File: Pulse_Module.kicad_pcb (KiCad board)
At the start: 2 copper layers, 61 parts, among them CON1 AVR-ISP-10, CON2 AVR-JTAG-10, CON3 BARREL_JACK, IC1 ATMEGA1280-A, P1 CONN_02X20, P2 USB_OTG, P3 CONN_01X03, P4 CONN_01X03, SW1 SW_PUSH, U1 74HCT541_PWR, U2 PL2303, U6 WS2812, U7 WS2812, U8 WS2812, X1 CRYSTAL, Y1 CRYSTAL

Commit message: Готовая плата версия_1
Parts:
- removed C15, C18: 0.1uF, Capacitors_SMD:C_0805
- removed R10: 150, Resistors_SMD:R_0402
- added C17: 0.1U, Capacitors_SMD:C_0805, F.Cu at (142.2, 117.8)
- moved P2 67.4 mm to (142.1, 145.7), turned to 0 degrees
- moved R3 62.8 mm to (143.2, 140.0), turned to 270 degrees
- moved C13 60.0 mm to (171.9, 134.2)
- moved D1 59.2 mm to (156.7, 134.0), turned to 90 degrees
- moved U7 58.2 mm to (185.6, 140.2), turned to 90 degrees
- moved U6 58.0 mm to (179.6, 140.2), turned to 90 degrees
- moved U8 57.9 mm to (173.6, 140.2), turned to 90 degrees
- moved R1 56.9 mm to (159.7, 134.1), turned to 90 degrees
- moved R4 56.3 mm to (140.2, 140.0), turned to 270 degrees
- moved D3 55.8 mm to (150.7, 134.0), turned to 90 degrees
- moved R5 55.7 mm to (146.0, 140.0), turned to 90 degrees
- moved C8 55.1 mm to (177.9, 134.2)
- moved R7 48.1 mm to (147.8, 134.1), turned to 90 degrees
- moved C7 47.4 mm to (183.9, 134.2), turned to 90 degrees
- moved R12 45.9 mm to (156.7, 129.7)
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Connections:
- net /Sheet56DEE0DD/17 renamed Net-(IC1-Pad35)
- C1 pad 1: /Vcc -> /Sheet56DEE0DD/Vcc
- C2 pad 1: /Vcc -> /Sheet56DEE0DD/Vcc
- CON1 pad 5: /Sheet56DEE0DD/RESET -> /Sheet56DEE0DD/Sheet570520A0/RESET
- Cff1 pad 1: /Vcc -> /Sheet56DEE0DD/Vcc
- IC1 pad 2: /Sheet56DEE0DD/RXD -> /Sheet56DEE0DD/Sheet570520A0/RXD
- IC1 pad 3: /Sheet56DEE0DD/TXD -> /Sheet56DEE0DD/Sheet570520A0/TXD
- IC1 pad 30: /Sheet56DEE0DD/RESET -> /Sheet56DEE0DD/Sheet570520A0/RESET
- JP2 pad 2: Net-(JP2-Pad2) -> /Sheet56D88A8D/FB
- JP2 pad 3: /Sheet56D88A8D/FB -> Net-(JP2-Pad3)
- L1 pad 2: /Vcc -> /Sheet56DEE0DD/Vcc
- P4 pad 2: /Sheet56DEE0DD/TXD -> /Sheet56DEE0DD/Sheet570520A0/TXD
- P4 pad 3: /Sheet56DEE0DD/RXD -> /Sheet56DEE0DD/Sheet570520A0/RXD
- R14 pad 1: /Vcc -> /Sheet56DEE0DD/Vcc
- R15 pad 1: Net-(JP2-Pad1) -> Net-(JP2-Pad3)
- R6 pad 2: /Sheet56DEE0DD/RESET -> /Sheet56DEE0DD/Sheet570520A0/RESET
- R9 pad 1: Net-(JP2-Pad2) -> Net-(JP2-Pad1)
- SW1 pad 2: /Sheet56DEE0DD/RESET -> /Sheet56DEE0DD/Sheet570520A0/RESET
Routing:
- net GND: track 1.59 -> 320.2 mm, vias 0 -> 21
- net +5V: track 166.9 -> 314.5 mm
- net /Sheet56DEE0DD/Sheet570520A0/RESET: track 0.00 -> 88.8 mm, vias 0 -> 5
- net /Sheet56DEE0DD/Dout: track 0.00 -> 81.4 mm, vias 0 -> 4
- net /Sheet56DEE0DD/Vcc: track 0.00 -> 68.3 mm
- net /Sheet56DEE0DD/CS: track 0.00 -> 65.0 mm, vias 0 -> 4
- net /Sheet56DEE0DD/Sheet570520A0/RXD: track 0.00 -> 57.2 mm, vias 0 -> 2
- net /Sheet56DEE0DD/Sheet570520A0/TXD: track 0.00 -> 55.6 mm, vias 0 -> 2
- net /Sheet56DEE0DD/40: track 0.00 -> 50.0 mm
- net Net-(IC1-Pad63): track 0.00 -> 50.0 mm, vias 0 -> 4
- net /Vcc: track 47.5 -> 0.00 mm, vias 4 -> 0
- net /Sheet56DEE0DD/Sheet570520A0/D+: track 0.00 -> 46.8 mm
- net /Sheet56DEE0DD/Sheet570520A0/D-: track 0.00 -> 45.7 mm
- net /Sheet56DEE0DD/38: track 0.00 -> 44.3 mm
- net /Sheet56DEE0DD/36: track 0.00 -> 43.3 mm, vias 0 -> 1
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- added copper zone on B.Cu, net GND
- added copper zone on F.Cu, net GND
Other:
- board outline added: 100.2 x 67.8 mm
- net class Pit added: clearance 0.1, trace_width 0.4, via_dia 0.6, via_drill 0.4
- net class Power added: clearance 0.1, trace_width 0.8, via_dia 0.6, via_drill 0.4

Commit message: Переразведённая лмка
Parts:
- added REF**: 1pin, Connect:1pin, F.Cu at (199.4, 81.9)
- moved REF** 186.6 mm to (106.7, 146.7)
- moved REF** 153.5 mm to (106.7, 81.9)
- moved REF** 102.8 mm to (199.4, 146.7)
- moved C1 27.4 mm to (127.1, 133.1), turned to 0 degrees
- moved D2 21.5 mm to (107.6, 118.0)
- moved C2 19.1 mm to (132.5, 107.4)
- moved LM2596 14.6 mm to (117.6, 105.3)
- moved R14 14.6 mm to (126.2, 103.5)
- moved Cff1 12.1 mm to (126.3, 99.9)
- moved L1 10.7 mm to (127.1, 118.5), turned to 0 degrees
- moved R15 9.08 mm to (112.6, 95.6)
- moved JP2 3.73 mm to (120.1, 92.8)
- moved CON3 2.18 mm to (117.6, 140.9)
- moved R9 1.83 mm to (127.4, 95.0), turned to 270 degrees
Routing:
- net /Sheet56D88A8D/FB: track 54.7 -> 23.1 mm
- net /Sheet56D88A8D/Vin: track 12.6 -> 26.2 mm
- net +5V: track 314.5 -> 304.0 mm, vias 0 -> 2
- net GND: track 320.2 -> 309.7 mm
- net Net-(D2-Pad2): track 22.2 -> 31.7 mm
- net (no net): track 9.41 -> 0.00 mm
- net /Sheet56DEE0DD/Vcc: track 68.3 -> 64.3 mm
- net Net-(JP2-Pad1): track 3.30 -> 5.26 mm
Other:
- board size 100.2 x 67.8 mm -> 100.2 x 70.9 mm

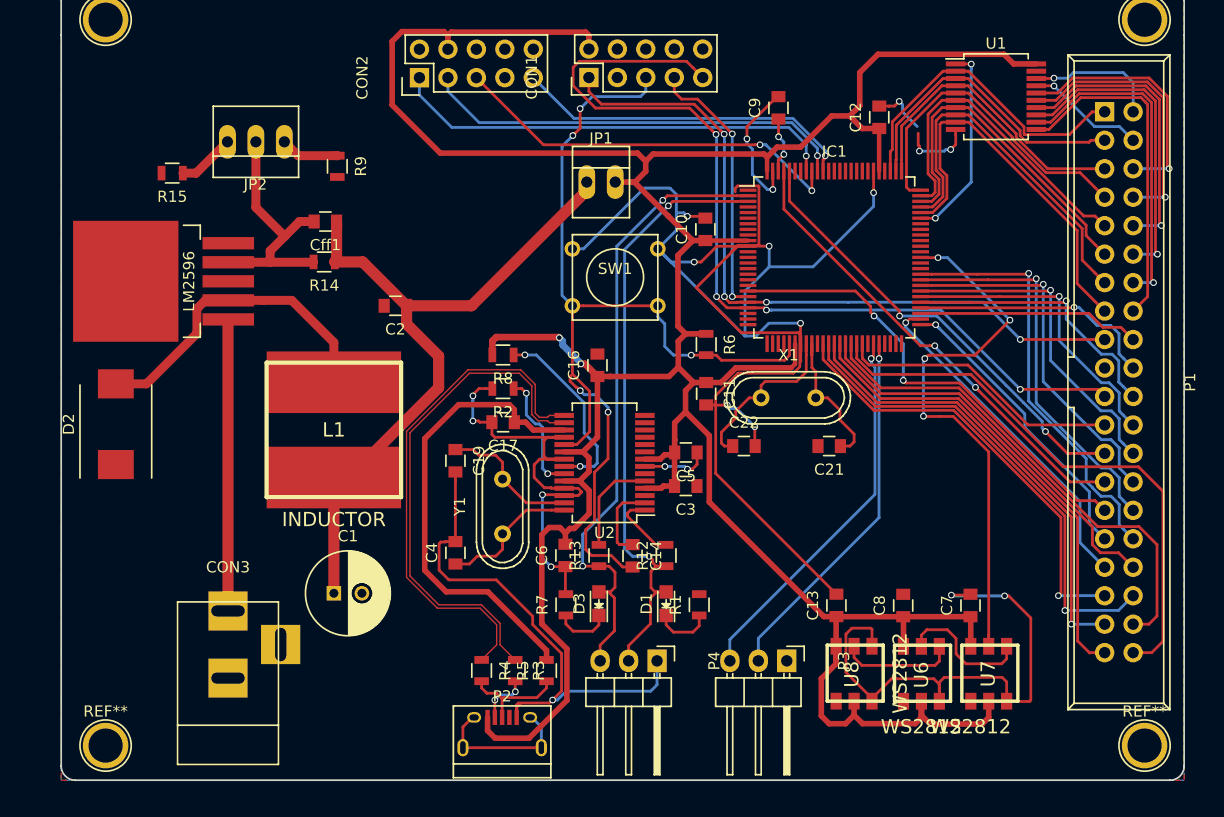
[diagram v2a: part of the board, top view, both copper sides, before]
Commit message: исправление согласно замечаниям, переразведена PL2303
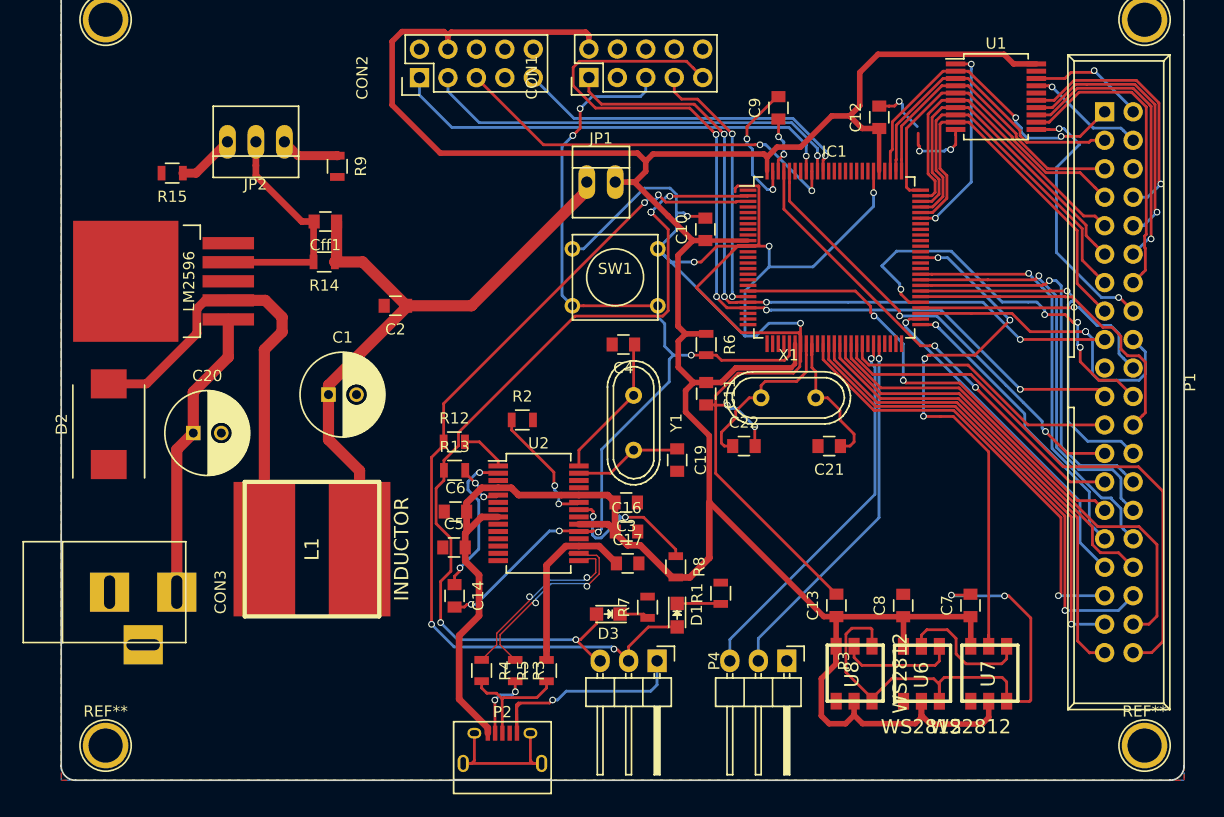
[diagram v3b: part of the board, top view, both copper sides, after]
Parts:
- added C20: 470uF, Capacitors_ThroughHole:C_Radial_D7.5_L11.2_P2.5, F.Cu at (114.5, 118.8)
- moved R8 24.4 mm to (157.6, 130.7), turned to 270 degrees
- moved C4 23.9 mm to (152.9, 110.9), turned to 180 degrees
- moved C5 22.4 mm to (137.8, 129.0), turned to 0 degrees
- moved R12 21.5 mm to (137.8, 119.6), turned to 0 degrees
- moved C19 19.8 mm to (157.7, 121.2)
- moved C1 17.7 mm to (126.6, 115.4)
- moved C17 16.8 mm to (153.3, 130.4), turned to 0 degrees
- moved C14 16.3 mm to (137.8, 133.3)
- moved C16 15.1 mm to (153.2, 127.6), turned to 0 degrees
- moved R13 15.0 mm to (137.8, 122.1), turned to 0 degrees
- moved Y1 13.9 mm to (153.8, 117.9), turned to 270 degrees
- moved CON3 13.3 mm to (106.8, 133.0), turned to 0 degrees
- moved L1 10.8 mm to (125.1, 129.2), turned to 90 degrees
- moved C6 10.6 mm to (137.9, 125.8), turned to 0 degrees
- moved U2 7.41 mm to (145.3, 126.0), turned to 0 degrees
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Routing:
- net GND: track 309.7 -> 235.8 mm, vias 21 -> 15
- net /Sheet56DEE0DD/Sheet570520A0/D+: track 46.8 -> 17.0 mm, vias 0 -> 2
- net /Sheet56DEE0DD/Sheet570520A0/D-: track 45.7 -> 18.5 mm, vias 0 -> 2
- net +3V3: track 41.7 -> 16.0 mm
- net /Sheet56DEE0DD/Sheet570520A0/TXD: track 55.6 -> 80.7 mm, vias 2 -> 4
- net /Sheet56DEE0DD/Sheet570520A0/RXD: track 57.2 -> 79.6 mm, vias 2 -> 5
- net /Sheet56DEE0DD/A2: track 22.7 -> 0.77 mm, vias 1 -> 0
- net +5V: track 304.0 -> 285.6 mm, vias 2 -> 0
- net Net-(D2-Pad2): track 31.7 -> 44.6 mm
- net /Sheet56DEE0DD/A10: track 24.6 -> 35.8 mm, vias 1 -> 4
- net /Sheet56DEE0DD/A8: track 19.9 -> 28.1 mm, vias 0 -> 2
- net Net-(C14-Pad1): track 7.17 -> 13.5 mm, vias 0 -> 2
- net /Sheet56DEE0DD/A7: track 30.3 -> 24.0 mm, vias 0 -> 2
- net /Sheet56DEE0DD/Vcc: track 64.3 -> 59.9 mm
- net Net-(R13-Pad2): track 8.95 -> 4.60 mm, vias 0 -> 2
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
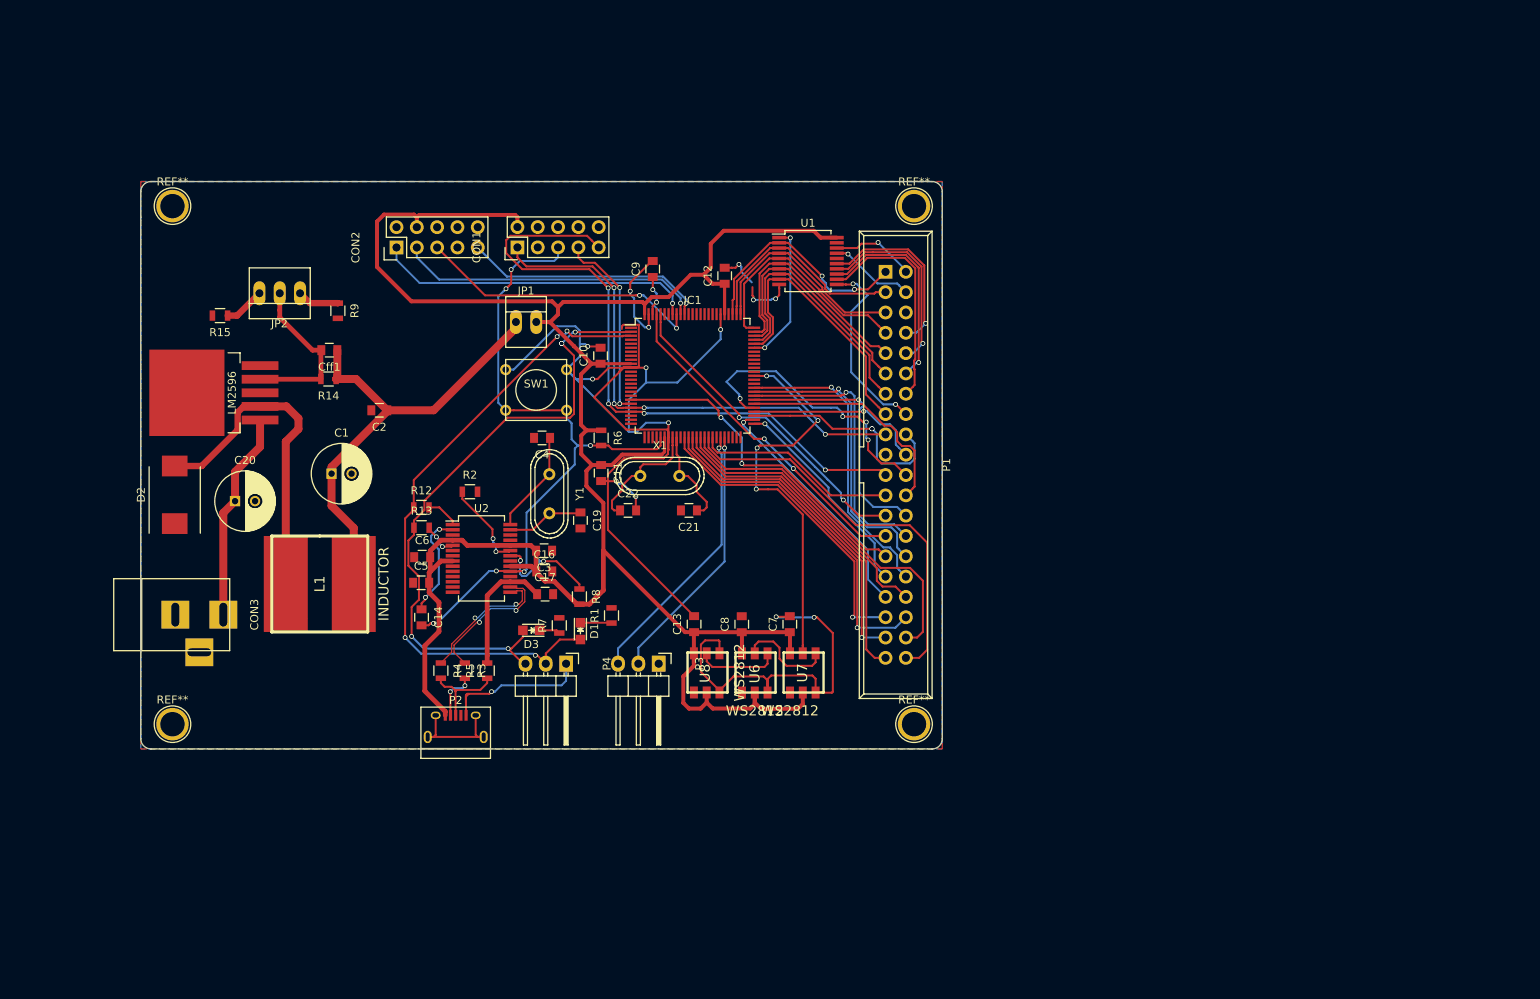
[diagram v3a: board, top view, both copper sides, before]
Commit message: подключение питания LMки от USB
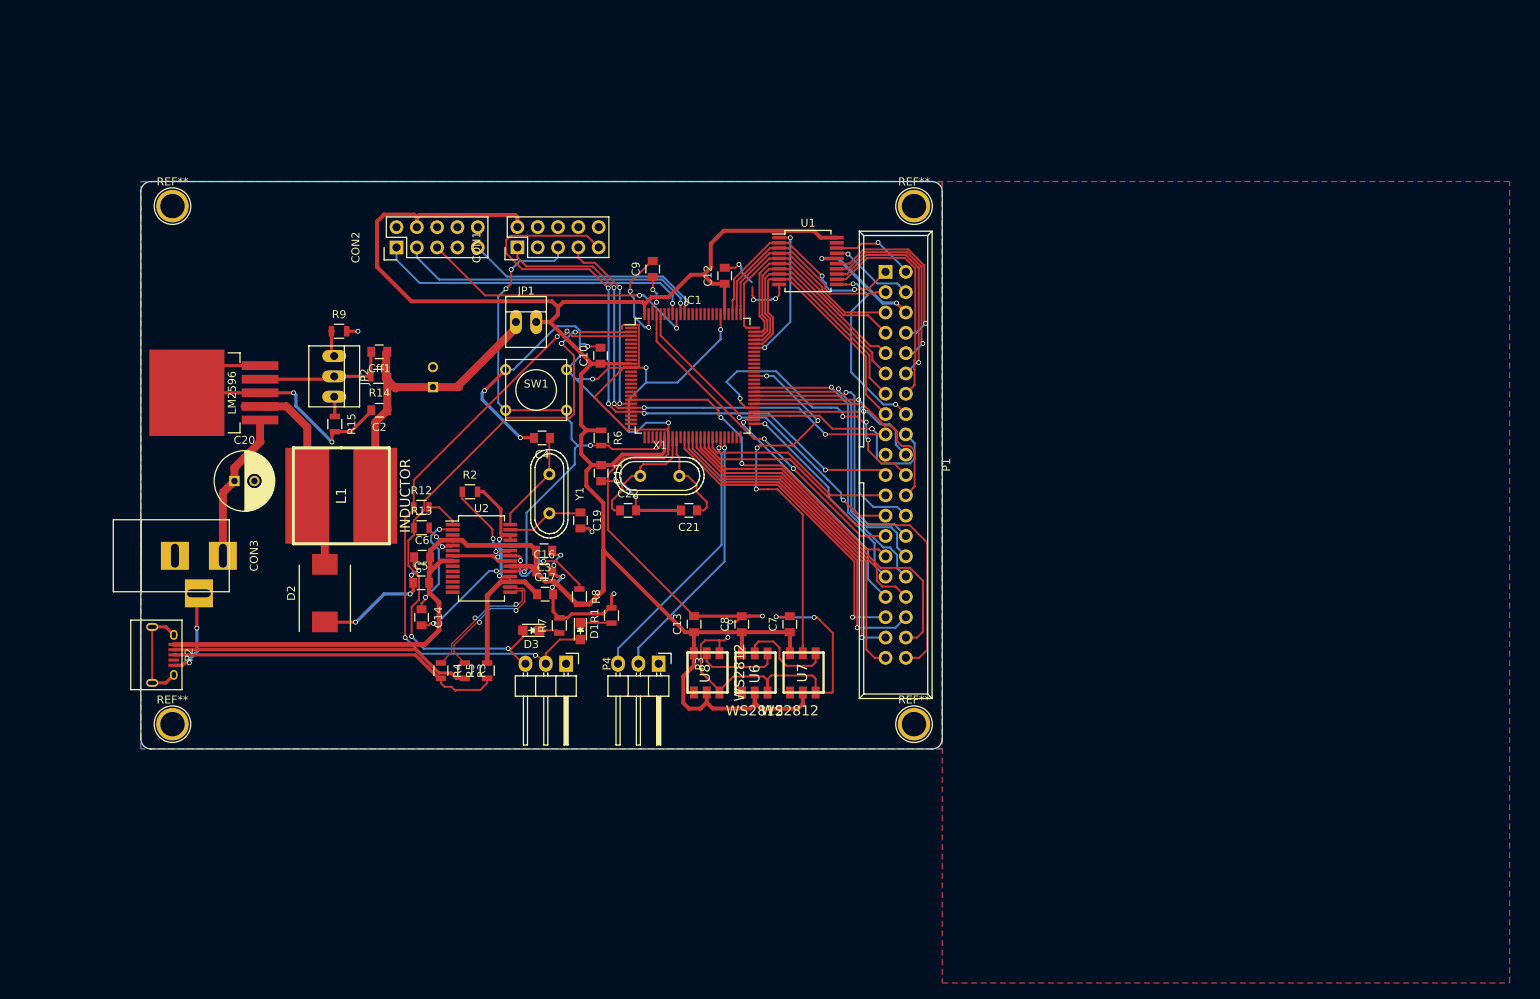
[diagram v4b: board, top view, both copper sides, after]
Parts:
- C1: moved to B.Cu
- moved P2 37.9 mm to (105.3, 138.0), turned to 270 degrees
- moved D2 22.4 mm to (125.7, 130.3)
- moved R15 19.7 mm to (127.0, 109.2), turned to 270 degrees
- moved C1 16.7 mm to (139.2, 104.5), turned to 90 degrees
- moved JP2 12.4 mm to (126.9, 103.2), turned to 270 degrees
- moved L1 11.3 mm to (127.8, 118.1)
- moved CON3 7.37 mm to (106.8, 125.6)
- moved R14 6.26 mm to (132.4, 103.2)
- moved Cff1 6.25 mm to (132.5, 100.1)
- moved R9 2.57 mm to (127.5, 97.6), turned to 0 degrees
- moved C20 2.52 mm to (114.4, 116.3)
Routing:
- net GND: track 235.8 -> 365.0 mm, vias 15 -> 37
- net Net-(P2-Pad2): track 6.04 -> 37.9 mm, vias 2 -> 0
- net Net-(P2-Pad3): track 10.9 -> 42.4 mm
- net +5V: track 285.6 -> 307.1 mm
- net /Sheet56DEE0DD/Vcc: track 59.9 -> 41.5 mm
- net /Sheet56DEE0DD/A2: track 0.77 -> 16.0 mm, vias 0 -> 2
- net Net-(D2-Pad2): track 44.6 -> 29.8 mm
- net /Sheet56D88A8D/Vin: track 26.5 -> 19.0 mm
- net /Sheet56D88A8D/FB: track 21.2 -> 17.1 mm
- net Net-(JP2-Pad3): track 5.17 -> 2.51 mm
- net Net-(JP2-Pad1): track 5.26 -> 3.26 mm
- net Net-(P2-Pad6): track 14.4 -> 13.5 mm

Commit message: Изменения футпринтов
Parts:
- added C23: C, Capacitors_SMD:C_0805, F.Cu at (119.9, 96.2)
- added C24: C, Capacitors_SMD:C_0805, F.Cu at (132.1, 94.5)
- added JP3: JUMPER, Connect:PINHEAD1-2, F.Cu at (125.5, 144.8)
- added JP4: JUMPER, Connect:PINHEAD1-2, F.Cu at (134.1, 144.8)
- added RV1: POT, Potentiometers:Potentiometer_Alps-RK163-single_15mm, F.Cu at (100.0, 93.5)
- added U3: AMS1117, TO_SOT_Packages_SMD:TO-252-2Lead, F.Cu at (125.6, 92.8)
- JP2: value JUMPER3 -> JUMPER
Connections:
- IC1 pad 42: /Sheet56DEE0DD/40 -> Net-(IC1-Pad42)
- JP2 pad 1: Net-(JP2-Pad1) -> /Sheet56DEE0DD/Vcc
- JP2 pad 2: /Sheet56D88A8D/FB -> Net-(C23-Pad1)
- JP2 pad 3: Net-(JP2-Pad3) -> (no net)
- P1 pad 40: /Sheet56DEE0DD/40 -> USB_IN
- P2 pad 1: +5V -> USB_IN
- U2 pad 20: +5V -> VCC
- U2 pad 24: +5V -> VCC
- U2 pad 8: +5V -> VCC
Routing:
- net /Sheet56DEE0DD/40: track 50.0 -> 0.00 mm
- net Net-(IC1-Pad42): track 0.00 -> 48.4 mm
- net +5V: track 307.1 -> 267.5 mm
- net USB_IN: track 0.00 -> 33.0 mm
- net VCC: track 0.00 -> 8.20 mm
- net Net-(JP2-Pad3): track 2.51 -> 0.00 mm
- net (no net): track 0.00 -> 2.51 mm
- net /Sheet56D88A8D/FB: track 17.1 -> 14.7 mm
- net Net-(C23-Pad1): track 0.00 -> 2.41 mm

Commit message: Последние изменения
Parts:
- removed R15: 1k, Resistors_SMD:R_0805
- removed R9: R, Resistors_SMD:R_0805
- C23: value C -> 10uF
- JP2: footprint Connect:PINHEAD1-3 -> Connect:PINHEAD1-2
- RV1: footprint Potentiometers:Potentiometer_Alps-RK163-single_15mm -> Potentiometers:Potentiometer_Bourns_3296W_3-8Zoll_Inline_ScrewUp
- moved JP2 21.0 mm to (108.0, 93.9)
- moved RV1 17.5 mm to (117.3, 96.2)
- moved C23 12.0 mm to (118.6, 84.2), turned to 0 degrees
- moved REF** 10.4 mm to (208.1, 152.4)
- moved REF** 9.37 mm to (99.7, 152.9)
- moved REF** 9.07 mm to (207.9, 78.8)
- moved REF** 7.95 mm to (99.4, 78.7)
- moved U3 2.24 mm to (125.5, 95.0)
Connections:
- net /Sheet56DEE0DD/34 renamed /Sheet56DEE0DD/А16
- net /Sheet56DEE0DD/35 renamed /Sheet56DEE0DD/Dout1
- net /Sheet56DEE0DD/37 renamed /Sheet56DEE0DD/CLK1
- net /Sheet56DEE0DD/39 renamed /Sheet56DEE0DD/CS1
- P1 pad 40: USB_IN -> /Sheet56DEE0DD/Vcc
- U2 pad 20: VCC -> USB_IN
- U2 pad 24: VCC -> USB_IN
- U2 pad 8: VCC -> USB_IN
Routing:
- net (no net): track 2.51 -> 236.6 mm
- net /Sheet56DEE0DD/Vcc: track 42.0 -> 184.1 mm, vias 0 -> 3
- net Net-(IC1-Pad42): track 48.4 -> 1.30 mm
- net USB_IN: track 33.0 -> 75.8 mm, vias 0 -> 4
- net /Sheet56D88A8D/Vin: track 19.0 -> 51.4 mm, vias 0 -> 2
- net GND: track 365.0 -> 344.2 mm, vias 37 -> 34
- net +5V: track 267.5 -> 286.9 mm, vias 0 -> 4
- net VCC: track 8.20 -> 0.00 mm
- net Net-(JP2-Pad1): track 2.78 -> 0.00 mm
- net /Sheet56D88A8D/FB: track 14.7 -> 17.1 mm
- net Net-(C23-Pad1): track 2.41 -> 0.00 mm
- removed copper zone on B.Cu, net GND
- removed copper zone on F.Cu, net GND
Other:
- board size 100.2 x 70.9 mm -> 7.6 x 5.7 mm

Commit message: Последние изменения на плате
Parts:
- removed RV1: POT, Potentiometers:Potentiometer_Bourns_3296W_3-8Zoll_Inline_ScrewUp
- added R10: 3k, Resistors_SMD:R_0805, F.Cu at (124.8, 100.8)
- added R11: 1k, Resistors_SMD:R_0805, F.Cu at (123.9, 106.0)
- added R9: R, Resistors_SMD:R_0805, F.Cu at (122.9, 82.8)
- added RV2: POT, Potentiometers:Potentiometer_Bourns_3296W_3-8Zoll_Inline_ScrewUp, F.Cu at (107.1, 86.5)
- moved REF** 5.46 mm to (94.8, 150.6)
- moved REF** 4.91 mm to (94.8, 80.5)
- moved REF** 3.52 mm to (205.0, 150.8)
- moved C23 3.50 mm to (119.3, 87.6)
- moved REF** 3.40 mm to (205.3, 81.0)
- moved JP2 1.66 mm to (109.5, 94.6), turned to 90 degrees
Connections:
- U3 pad 1: GND -> Net-(R9-Pad2)
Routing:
- net (no net): track 236.6 -> 0.00 mm
- net Net-(C23-Pad1): track 0.00 -> 30.1 mm
- net Net-(R9-Pad2): track 0.00 -> 22.7 mm
- net /Sheet56DEE0DD/Vcc: track 184.1 -> 163.6 mm
- net +5V: track 286.9 -> 295.1 mm
- net /Sheet56D88A8D/FB: track 17.1 -> 23.7 mm
- net USB_IN: track 75.8 -> 81.6 mm
- net Net-(IC1-Pad42): track 1.30 -> 0.00 mm
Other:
- board size 7.6 x 5.7 mm -> 124.8 x 83.6 mm
